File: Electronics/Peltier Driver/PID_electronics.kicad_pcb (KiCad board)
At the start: 2 copper layers, 81.3 x 45.7 mm, 15 parts, among them J1 Conn_01x05, J2 Conn_01x03, Q3 2N7000, U1 LF412

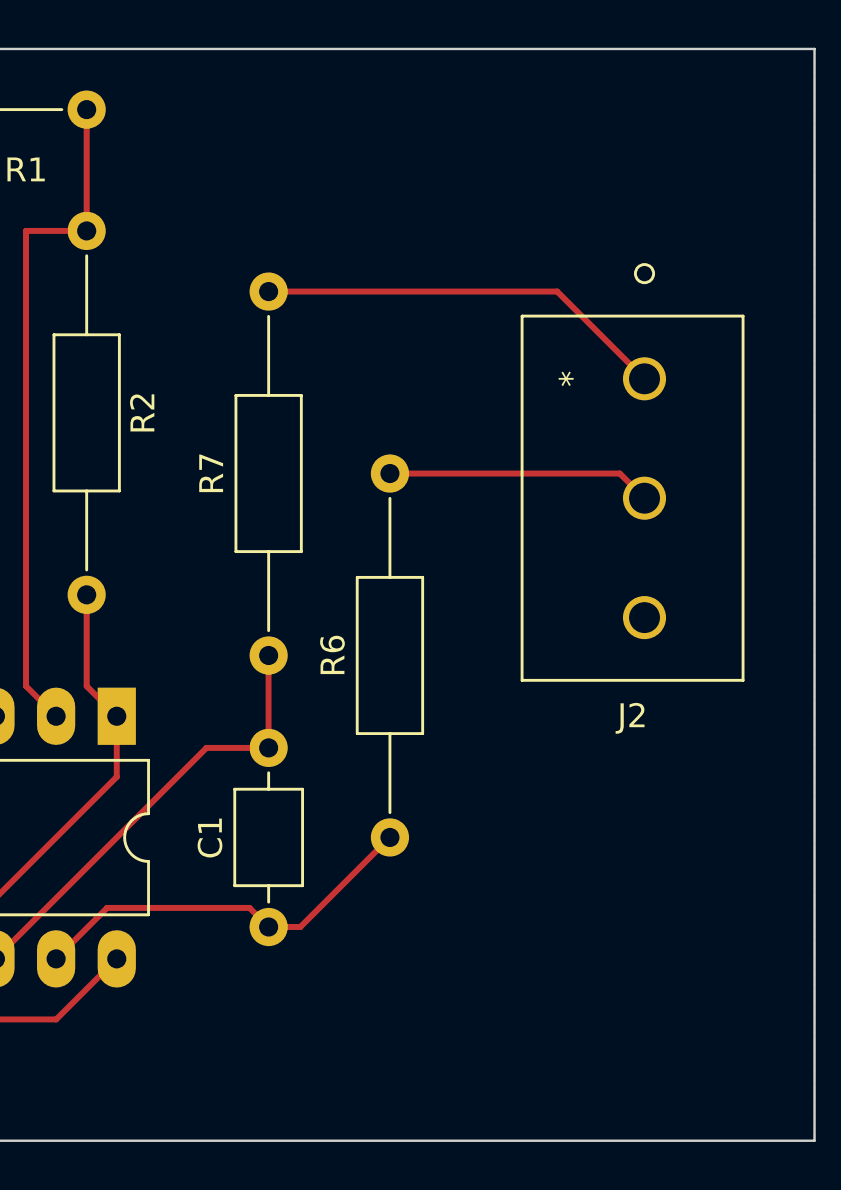
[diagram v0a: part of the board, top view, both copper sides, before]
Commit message: updated silkscreen
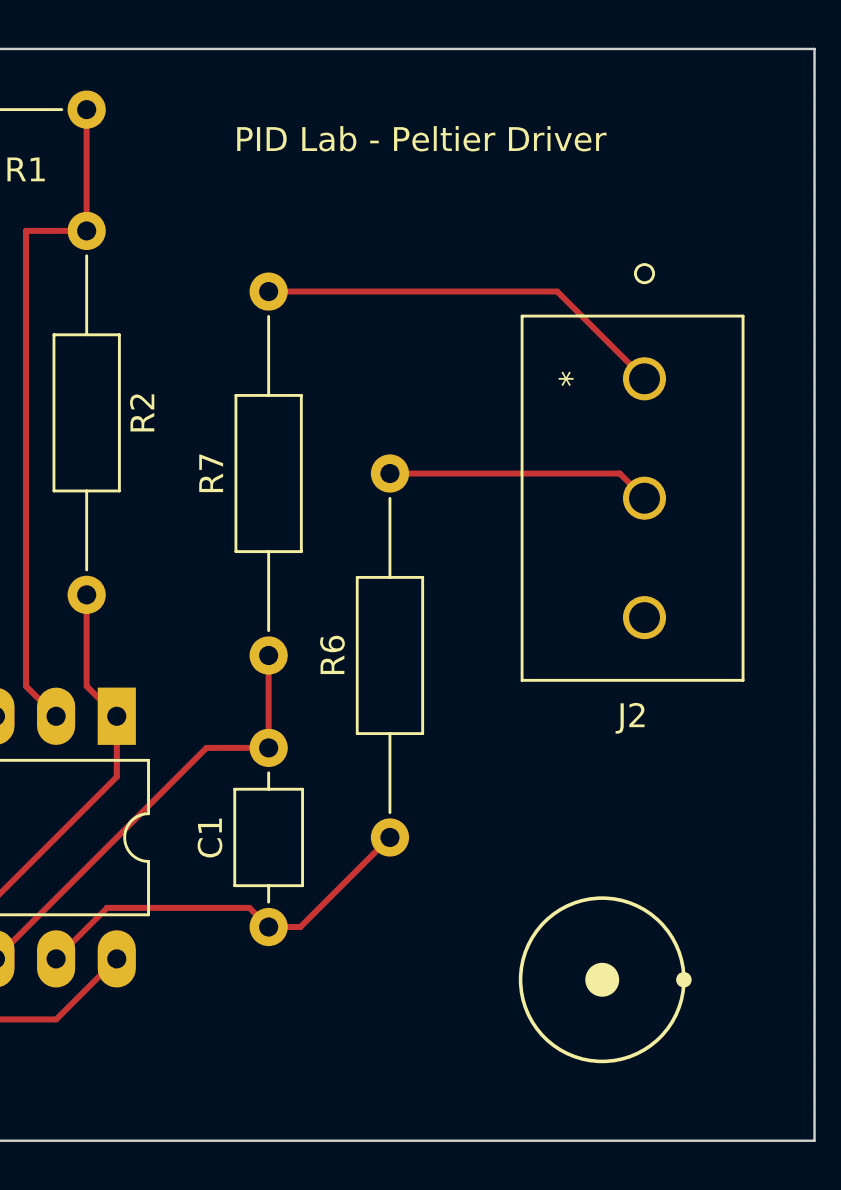
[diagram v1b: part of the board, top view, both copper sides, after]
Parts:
- R4: value 10K -> 100K
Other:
- board text added: "PID Lab - Peltier Driver"

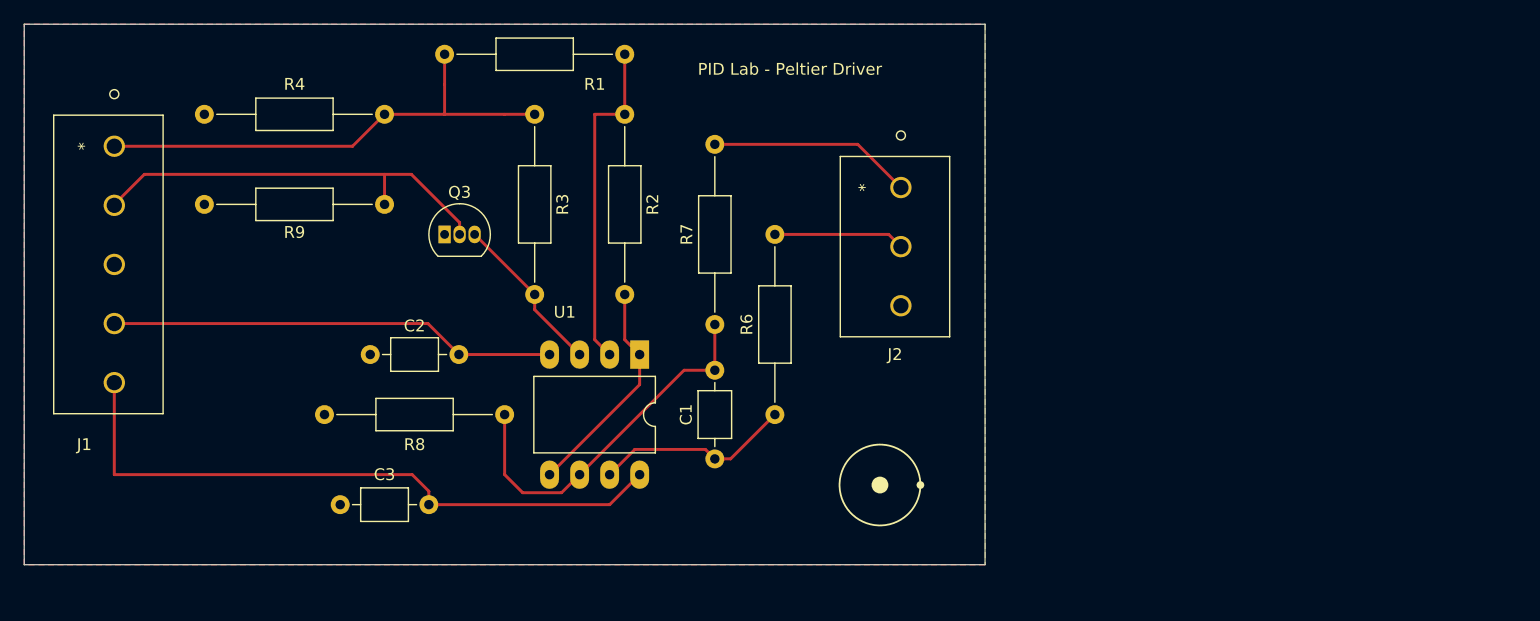
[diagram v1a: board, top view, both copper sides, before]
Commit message: Added mounting holes
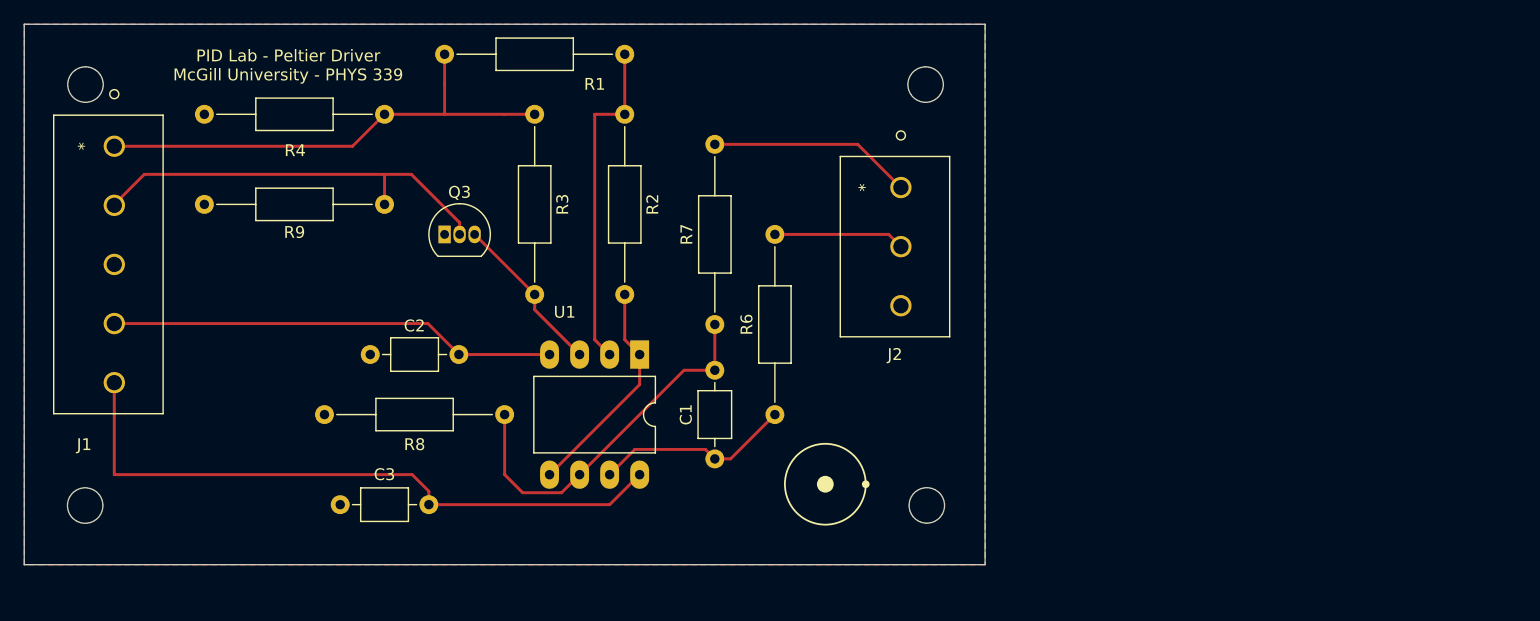
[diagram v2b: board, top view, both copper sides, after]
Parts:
- added REF**: mounting hole, KiCAD_footprints:mounting hole, F.Cu at (83.9, 76.2)
- added REF**: mounting hole, KiCAD_footprints:mounting hole, F.Cu at (155.0, 76.2)
- added REF**: mounting hole, KiCAD_footprints:mounting hole, F.Cu at (83.9, 111.8)
- added REF**: mounting hole, KiCAD_footprints:mounting hole, F.Cu at (155.1, 111.8)
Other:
- board text added: "PID Lab - Peltier Driver McGill University - PHYS 339"
- board text removed: "PID Lab - Peltier Driver"
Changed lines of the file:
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@@
       (net 4 "GNDREF") (pinfunction "Pin_3") (pintype "passive"))
+  )
+  (footprint "KiCAD_footprints:mounting hole" (layer "F.Cu")
+    (at 83.9216 76.2254)
+    (attr through_hole)
+    (fp_text reference "REF**" (at 0 -0.5 unlocked) (layer "F.SilkS") hide
+      (effects (font (size 1 1) (thickness 0.15)))
+    )
+    (fp_text value "mounting hole" (at 0 1 unlocked) (layer "F.Fab") hide
+      (effects (font (size 1 1) (thickness 0.15)))
+    )
+    (fp_text user "${REFERENCE}" (at 0 2.5 unlocked) (layer "F.Fab") hide
+      (effects (font (size 1 1) (thickness 0.15)))
+    )
+    (pad "" np_thru_hole circle (at 0 -5.08) (size 3 3) (drill 3) (layers *.Mask))
   )
   (footprint "Package_TO_SOT_THT:TO-92_Inline" (layer "F.Cu")
@@
       (rotate (xyz 0 0 0))
     )
+  )
+  (footprint "KiCAD_footprints:mounting hole" (layer "F.Cu")
+    (at 154.9908 76.2254)
+    (attr through_hole)
+    (fp_text reference "REF**" (at 0 -0.5 unlocked) (layer "F.SilkS") hide
+      (effects (font (size 1 1) (thickness 0.15)))
+    )
+    (fp_text value "mounting hole" (at 0 1 unlocked) (layer "F.Fab") hide
+      (effects (font (size 1 1) (thickness 0.15)))
+    )
+    (fp_text user "${REFERENCE}" (at 0 2.5 unlocked) (layer "F.Fab") hide
+      (effects (font (size 1 1) (thickness 0.15)))
+    )
+    (pad "" np_thru_hole circle (at 0 -5.08) (size 3 3) (drill 3) (layers *.Mask))
   )
   (footprint "KiCAD_footprints:1935190" (layer "F.Cu")
@@
     (property "Sheetname" "")
     (attr through_hole)
-    (fp_text reference "R4" (at 7.62 2.54) (layer "F.SilkS")
+    (fp_text reference "R4" (at 7.5692 -3.0734) (layer "F.SilkS")
       (effects (font (size 1 1) (thickness 0.15)))
     )
@@
     )
   )
+  (footprint "KiCAD_footprints:mounting hole" (layer "F.Cu")
+    (at 83.8962 111.8362)
+    (attr through_hole)
+    (fp_text reference "REF**" (at 0 -0.5 unlocked) (layer "F.SilkS") hide
+      (effects (font (size 1 1) (thickness 0.15)))
+    )
+    (fp_text value "mounting hole" (at 0 1 unlocked) (layer "F.Fab") hide
+      (effects (font (size 1 1) (thickness 0.15)))
+    )
+    (fp_text user "${REFERENCE}" (at 0 2.5 unlocked) (layer "F.Fab") hide
+      (effects (font (size 1 1) (thickness 0.15)))
+    )
+    (pad "" np_thru_hole circle (at 0 -5.08) (size 3 3) (drill 3) (layers *.Mask))
+  )
   (footprint "Capacitor_THT:C_Axial_L3.8mm_D2.6mm_P7.50mm_Horizontal" (layer "F.Cu")
     (at 108.01 93.98)
@@
     )
   )
+  (footprint "KiCAD_footprints:mounting hole" (layer "F.Cu")
+    (at 155.0924 111.8262)
+    (attr through_hole)
+    (fp_text reference "REF**" (at 0 -0.5 unlocked) (layer "F.SilkS") hide
+      (effects (font (size 1 1) (thickness 0.15)))
+    )
+    (fp_text value "mounting hole" (at 0 1 unlocked) (layer "F.Fab") hide
+      (effects (font (size 1 1) (thickness 0.15)))
+    )
+    (fp_text user "${REFERENCE}" (at 0 2.5 unlocked) (layer "F.Fab") hide
+      (effects (font (size 1 1) (thickness 0.15)))
+    )
+    (pad "" np_thru_hole circle (at 0 -5.08) (size 3 3) (drill 3) (layers *.Mask))
+  )
   (footprint "Resistor_THT:R_Axial_DIN0207_L6.3mm_D2.5mm_P15.24mm_Horizontal" (layer "F.Cu")
     (at 142.24 99.06 90)
@@
     )
   )
-  (gr_circle (center 151.13 105.019579) (end 151.765 105.019579) (layer "F.SilkS") (width 0.15) (fill solid))
-  (gr_circle (center 154.549579 105.019579) (end 154.799579 105.019579) (layer "F.SilkS") (width 0.15) (fill solid))
-  (gr_circle (center 151.13 105.019579) (end 149.86 108.194579) (layer "F.SilkS") (width 0.15) (fill none))
+  (gr_circle (center 146.5072 104.9528) (end 147.1422 104.9528) (layer "F.SilkS") (width 0.15) (fill solid))
+  (gr_circle (center 149.926779 104.9528) (end 150.176779 104.9528) (layer "F.SilkS") (width 0.15) (fill solid))
+  (gr_circle (center 146.5072 104.9528) (end 145.2372 108.1278) (layer "F.SilkS") (width 0.15) (fill none))
   (gr_line (start 160.02 66.04) (end 160.02 111.76) (layer "Edge.Cuts") (width 0.1))
   (gr_line (start 160.02 111.76) (end 78.74 111.76) (layer "Edge.Cuts") (width 0.1))
   (gr_line (start 78.74 66.04) (end 160.02 66.04) (layer "Edge.Cuts") (width 0.1))
   (gr_line (start 78.74 111.76) (end 78.74 66.04) (layer "Edge.Cuts") (width 0.1))
-  (gr_text "PID Lab - Peltier Driver" (at 143.51 69.85) (layer "F.SilkS")
+  (gr_text "PID Lab - Peltier Driver\nMcGill University - PHYS 339" (at 101.0666 69.5198) (layer "F.SilkS")
     (effects (font (size 1 1) (thickness 0.15)))
   )

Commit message: Board revision
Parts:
- removed REF** (x4): mounting hole, KiCAD_footprints:mounting hole
- C1: value 100 pF -> 10 nF
- C2, C3: value 100 nF -> 1 uF
- R1, R2, R3, R4, R6, R9: footprint Resistor_THT:R_Axial_DIN0207_L6.3mm_D2.5mm_P15.24mm_Horizontal -> Resistor_THT:R_Axial_DIN0207_L6.3mm_D2.5mm_P10.16mm_Horizontal
- R7, R8: value 20K -> 10K; footprint Resistor_THT:R_Axial_DIN0207_L6.3mm_D2.5mm_P15.24mm_Horizontal -> Resistor_THT:R_Axial_DIN0207_L6.3mm_D2.5mm_P10.16mm_Horizontal
- moved R8 22.8 mm to (135.0, 82.4), turned to -90 degrees
- moved C3 18.0 mm to (130.7, 109.4)
- moved R7 11.9 mm to (134.9, 79.8), turned to 0 degrees
- moved R1 7.60 mm to (111.6, 75.7)
- moved R9 6.84 mm to (110.3, 88.0)
- moved R4 5.39 mm to (109.0, 79.0)
- moved R2 5.11 mm to (129.5, 78.8)
- moved R3 4.95 mm to (121.9, 78.6)
- moved J1 4.11 mm to (90.5, 76.3)
- moved C2 3.91 mm to (111.9, 94.0)
- moved R6 1.71 mm to (143.9, 98.9)
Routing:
- net Net-(J2-Pad1): track 17.3 -> 7.89 mm
- net Net-(J1-Pad1): track 41.8 -> 35.6 mm
- net Net-(J1-Pad2): track 35.5 -> 30.2 mm
- net -15V: track 37.9 -> 33.8 mm
- net +15V: track 55.0 -> 51.1 mm
- net Net-(C1-Pad1): track 16.7 -> 18.5 mm
- net Net-(C1-Pad2): track 31.7 -> 33.2 mm
- net Net-(R1-Pad2): track 28.5 -> 27.4 mm
- added copper zone on B.Cu, net GNDREF
- removed copper zone on F.Cu, net GNDREF
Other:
- board size 81.3 x 45.7 mm -> 79.1 x 42 mm
- board text added: "+15V"
- board text added: "-15V"
- board text added: "FDBK"
- board text added: "GNDREF"
- board text added: "OUT"
- board text added: "POL"
- board text added: "SGNL"

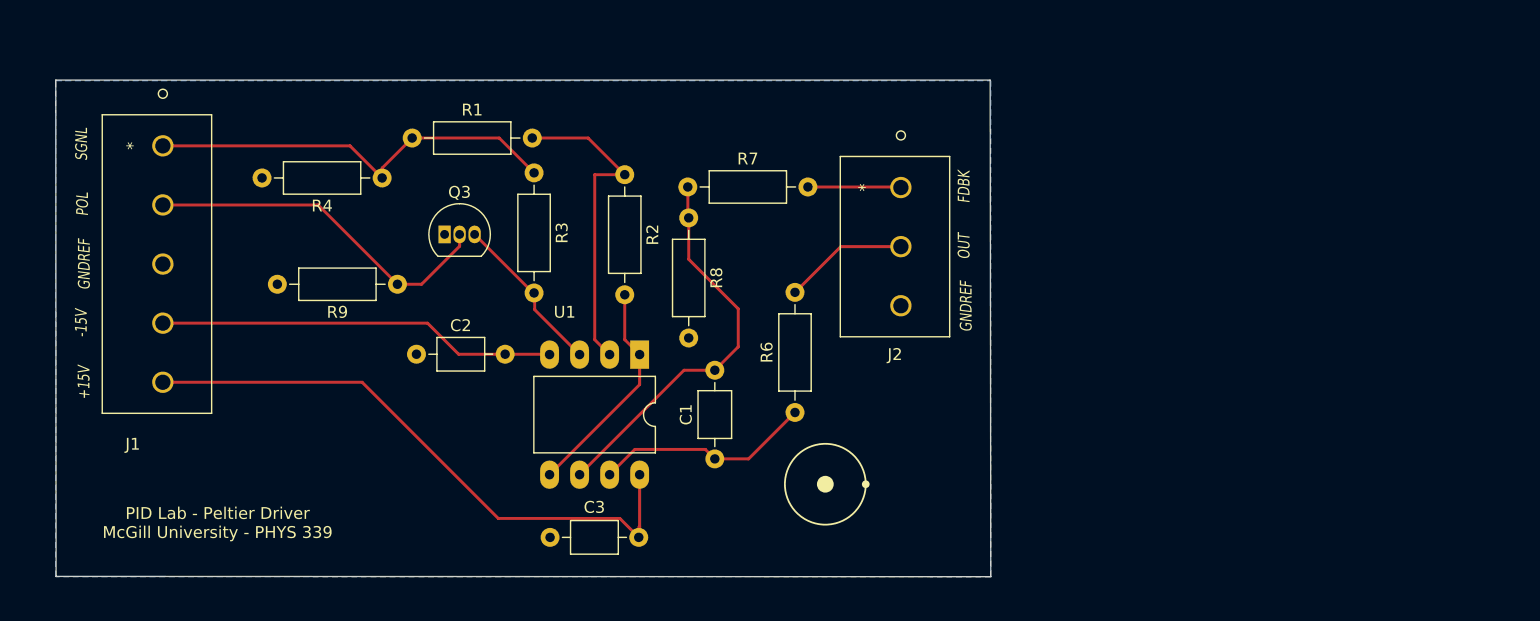
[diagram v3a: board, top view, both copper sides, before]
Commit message: Added Bulk decoupling capacitors and optional snubber network
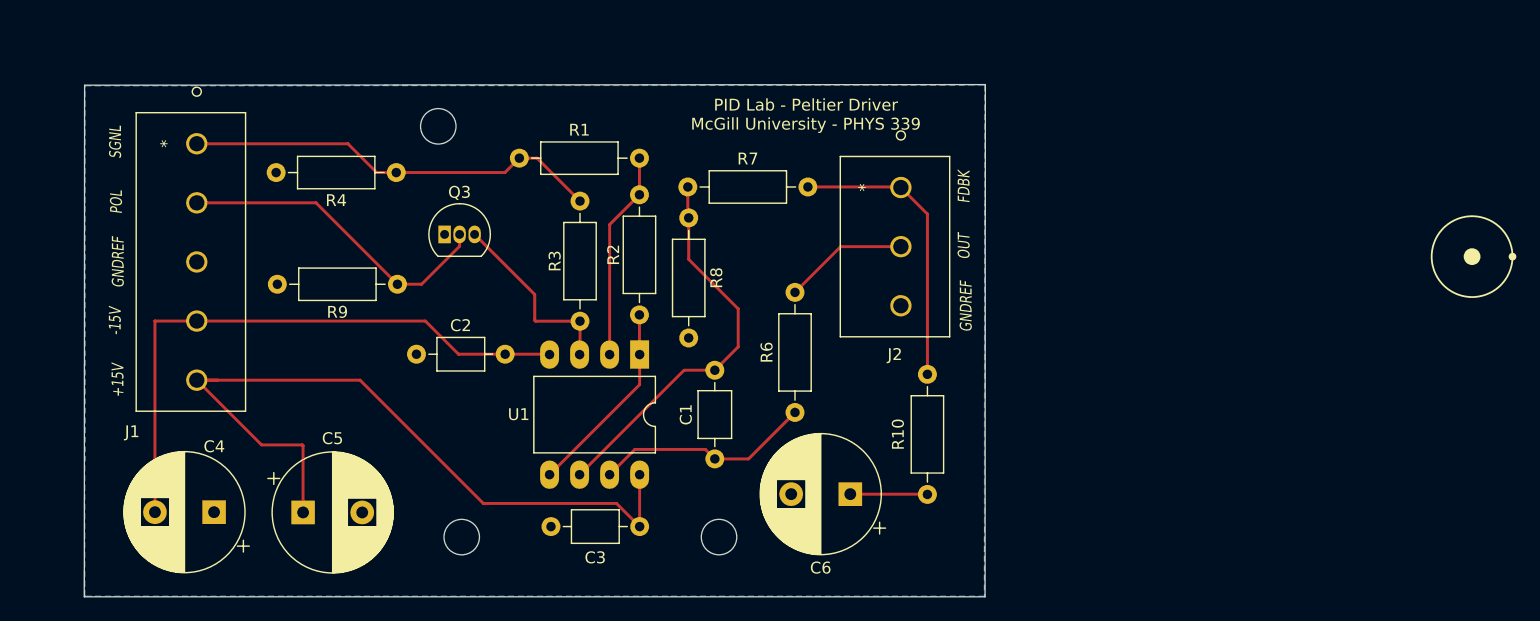
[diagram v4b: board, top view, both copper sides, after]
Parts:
- added C4: 1000 uF, Capacitor_THT:CP_Radial_D10.0mm_P5.00mm, F.Cu at (94.8, 107.3)
- added C5: 1000 uF, Capacitor_THT:CP_Radial_D10.0mm_P5.00mm, F.Cu at (102.3, 107.3)
- added C6: C_Small, Capacitor_THT:CP_Radial_D10.0mm_P5.00mm, F.Cu at (148.6, 105.8)
- added R10: R, Resistor_THT:R_Axial_DIN0207_L6.3mm_D2.5mm_P10.16mm_Horizontal, F.Cu at (155.1, 95.7)
- added REF**: mounting hole, KiCAD_footprints:mounting hole, F.Cu at (115.7, 114.5)
- added REF**: mounting hole, KiCAD_footprints:mounting hole, F.Cu at (113.8, 79.8)
- added REF**: mounting hole, KiCAD_footprints:mounting hole, F.Cu at (137.5, 114.5)
- C1: value 10 nF -> 1 nF
- moved R1 9.23 mm to (120.6, 77.4)
- moved R3 4.56 mm to (125.8, 81.0)
- moved J1 2.88 mm to (93.3, 76.1)
- moved R2 2.11 mm to (130.8, 80.5)
- moved R4 1.28 mm to (110.2, 78.6)
- moved C3 0.92 mm to (130.8, 108.5)
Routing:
- net -15V: track 33.8 -> 50.7 mm
- net Net-(J2-Pad1): track 7.89 -> 24.6 mm
- net +15V: track 51.1 -> 65.8 mm
- net Net-(R1-Pad2): track 27.4 -> 17.7 mm
- net Net-(R10-Pad2): track 0.00 -> 6.53 mm
- net Net-(J1-Pad2): track 30.2 -> 27.4 mm
- net Net-(R2-Pad2): track 18.9 -> 16.7 mm
- net Net-(Q3-Pad3): track 13.8 -> 16.1 mm
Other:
- board size 79.1 x 42 mm -> 76.2 x 43.3 mm

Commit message: Added additional optional bypass capacitors
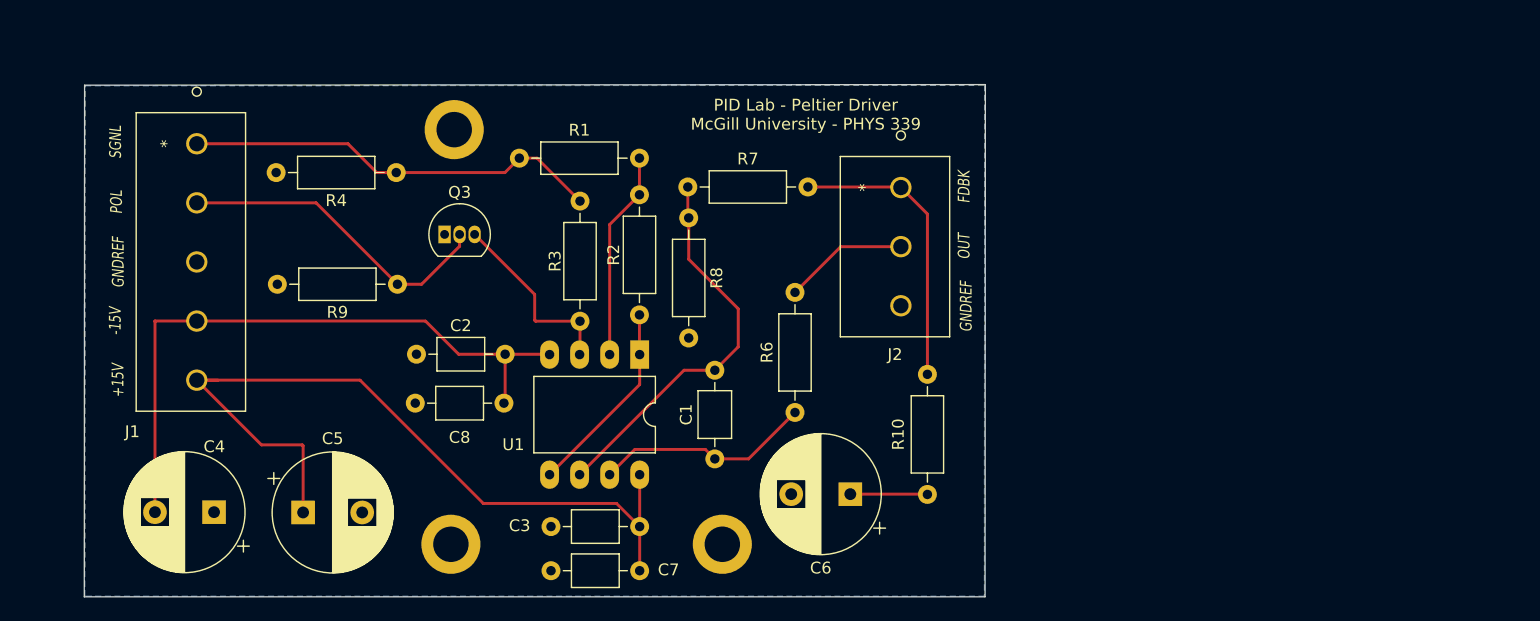
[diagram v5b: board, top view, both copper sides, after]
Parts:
- removed REF** (x3): mounting hole, KiCAD_footprints:mounting hole
- added ?: , , F.Cu at (115.1, 75.0)
- added ?: , , F.Cu at (137.8, 109.5)
- added ?: , , F.Cu at (114.8, 110.0)
- added C7: C_Small, Capacitor_THT:C_Axial_L3.8mm_D2.6mm_P7.50mm_Horizontal, F.Cu at (130.8, 112.3)
- added C8: C_Small, Capacitor_THT:C_Axial_L3.8mm_D2.6mm_P7.50mm_Horizontal, F.Cu at (111.8, 98.1)
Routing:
- net -15V: track 50.7 -> 54.9 mm
- net +15V: track 65.8 -> 69.5 mm
